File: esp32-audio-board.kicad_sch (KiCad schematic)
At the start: 130 parts, among them IC1 LP2985A-33DBVR, J10 PWR_LED+, J2 JST S2B, J21 IO32_PAD0, J22 PWR_LED-, J23 CHG_LED+, J24 CHG_LED-, J3 USB_C_Receptacle_USB2.0_16P, J5 IO32_PAD1, J6 IO33_PAD0, J7 IO33_PAD1, J8 IO25_PAD0, J9 IO25_PAD1, Q1 SS8050, Q2 SS8050, Q4 AO3401A, U1 ESP32-WROOM-32E, U2 CP2102, U3 MCP73831-2-OT, U5 ES8388

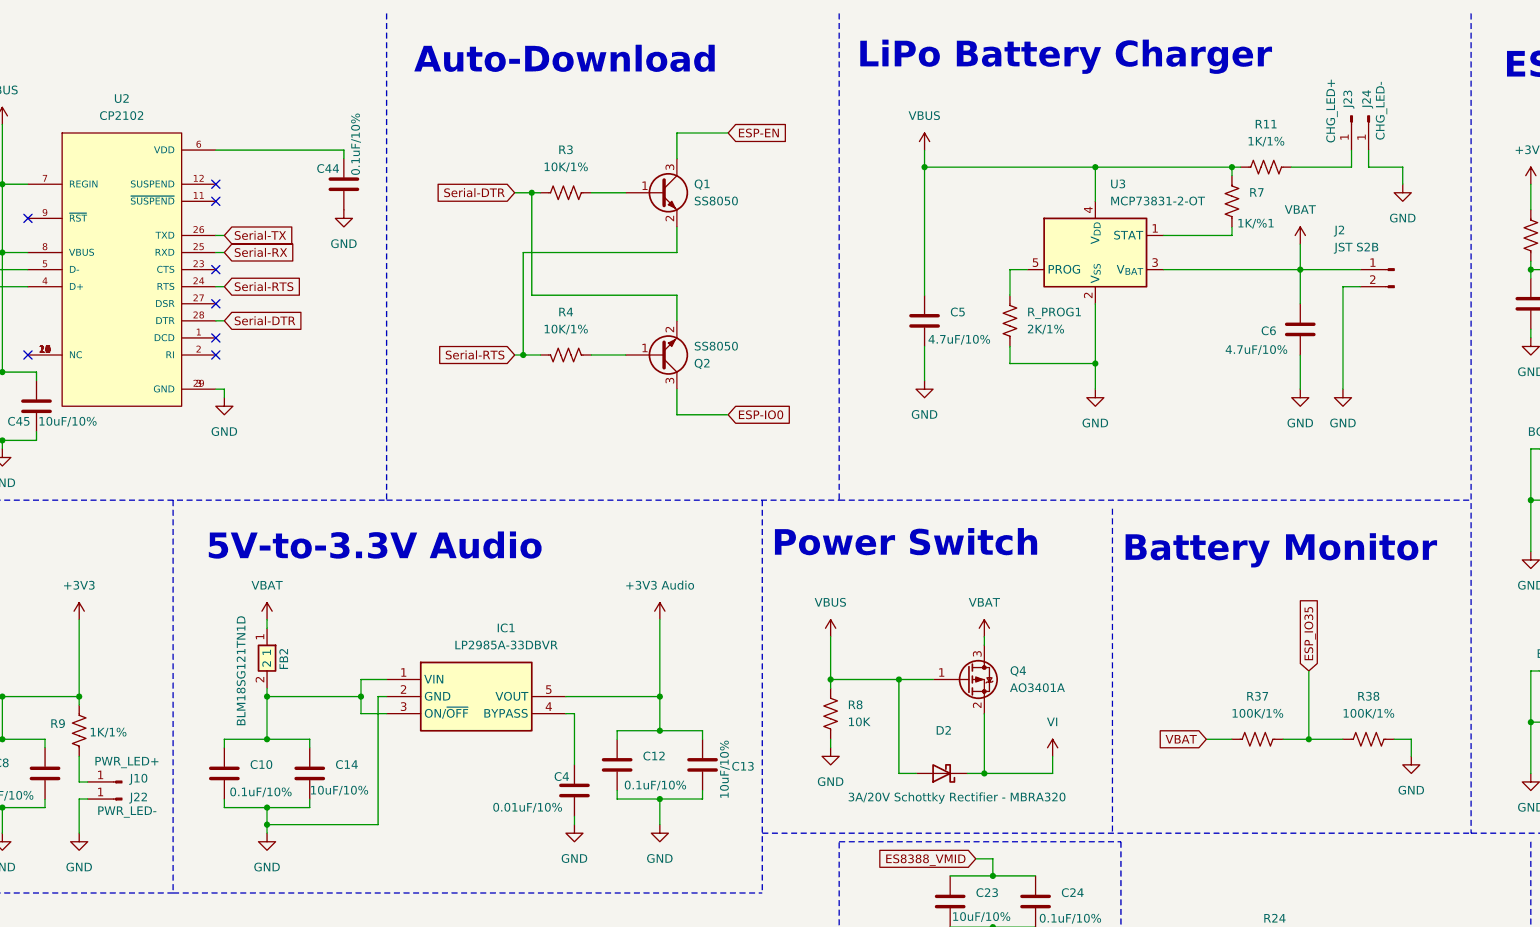
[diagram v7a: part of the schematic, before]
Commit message: esp32-audio-board: fix VI for audio pwr
The audio 3V3 was coming directly from the battery, which
may not be present and the VBUS should power the audio
circuits. The production board has this problem, but it
should not be affected if a battery is plugged in, as
the battery voltage will be present and the battery will
power the audio circuits correctly even when charging.

The charging led is now hooked correctly to the charger
IC on the STAT pin.

Signed-off-by: RaresCon <rares.constantin2002@gmail.com>
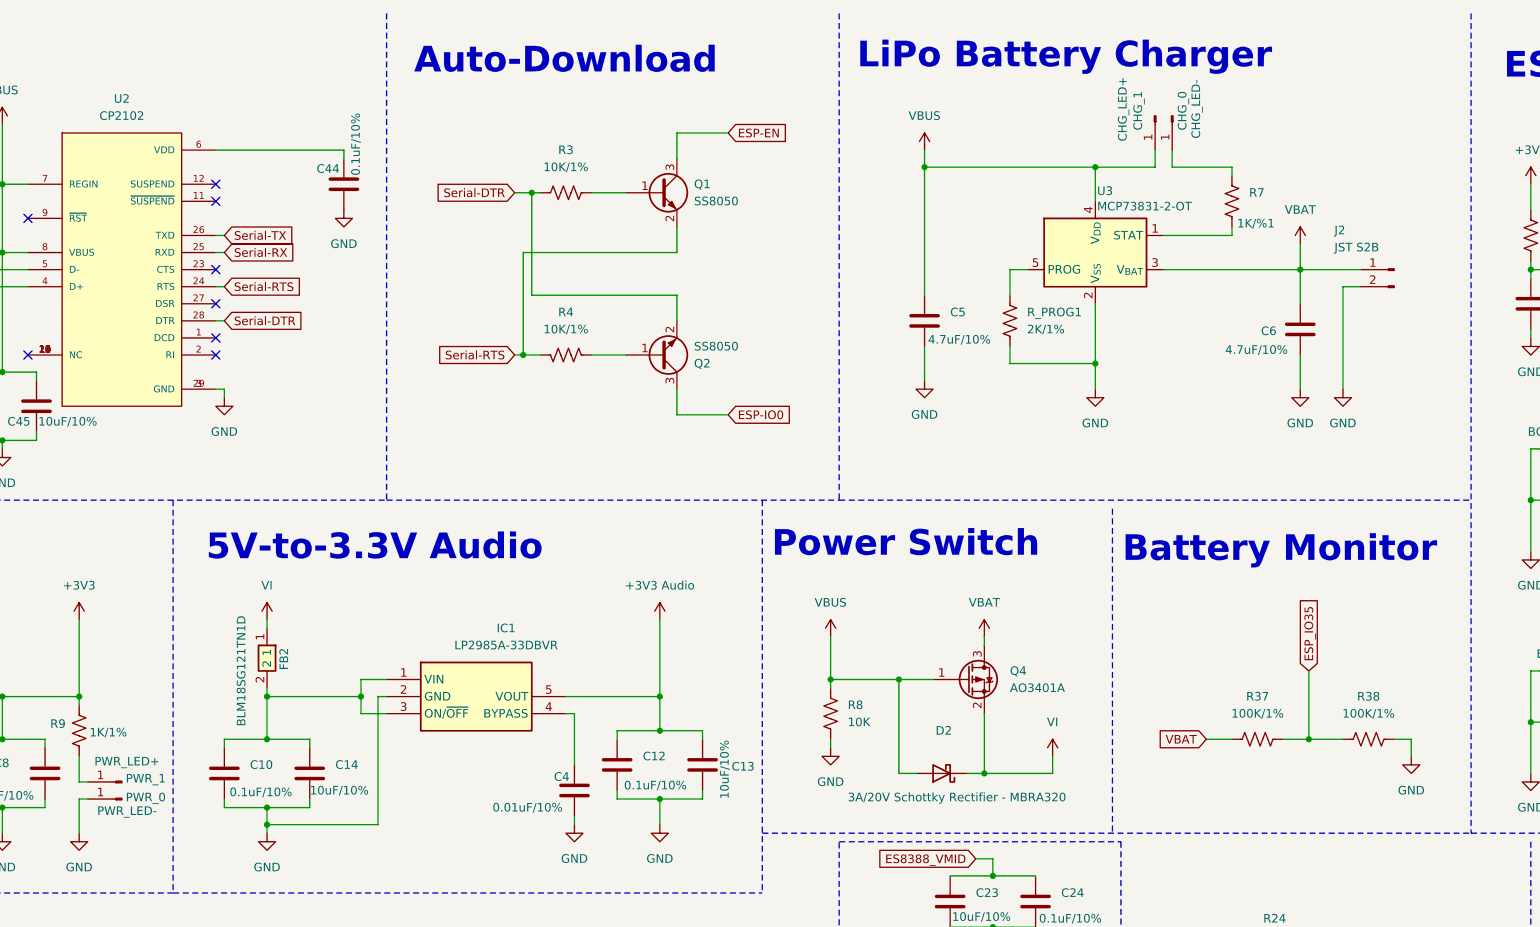
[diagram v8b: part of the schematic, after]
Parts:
- removed R11: 1K/1%, Resistor_SMD:R_0402_1005Metric_Pad0.72x0.64mm_HandSolder, symbol Device:R_US
- renumbered J24 to CHG_0, J23 to CHG_1, J22 to PWR_0, J10 to PWR_1
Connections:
- net GND: no longer CHG_0.1 (Pin_1)
- net VBAT: no longer FB2.1
- net VBUS: now also CHG_1.1 (Pin_1); no longer R7.2
- net VI: now also FB2.1
- new net: CHG_0.1 (Pin_1), R7.2
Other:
- moved on the sheet: CHG_0, CHG_1
